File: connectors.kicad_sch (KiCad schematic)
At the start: 4 parts

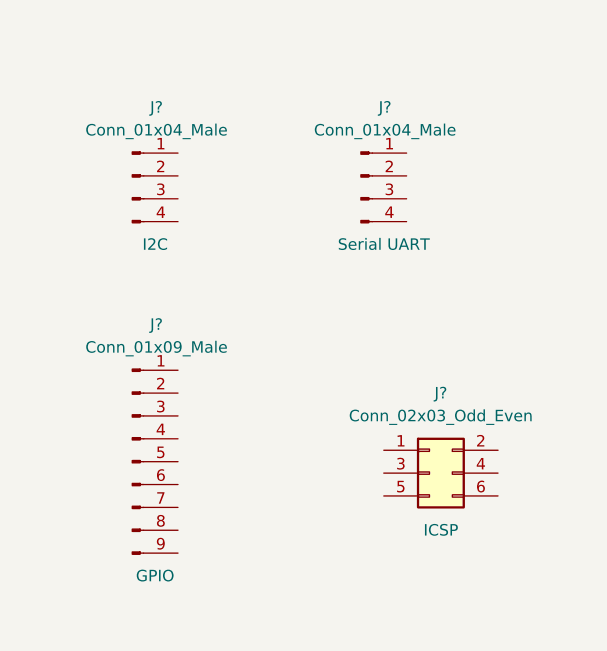
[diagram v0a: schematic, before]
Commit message: Changed locations of symbols (arrange).
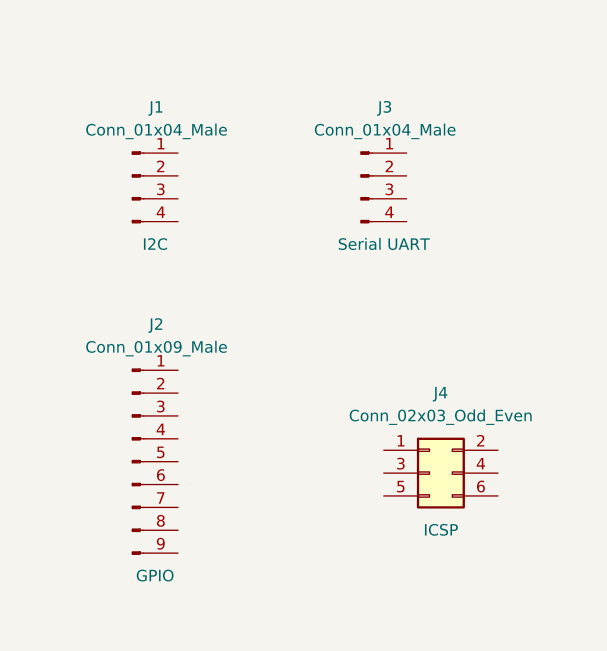
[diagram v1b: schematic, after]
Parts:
- gave numbers to parts that had none: 4
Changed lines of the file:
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@@
   (symbol (lib_id "Connector:Conn_01x04_Male") (at 116.84 78.74 0) (unit 1)
     (in_bom yes) (on_board yes)
-    (property "Reference" "J?" (id 0) (at 119.5324 71.12 0))
+    (property "Reference" "J1" (id 0) (at 119.5324 71.12 0))
     (property "Value" "Conn_01x04_Male" (id 1) (at 119.5324 73.66 0))
     (property "Footprint" "" (id 2) (at 116.84 78.74 0)
@@
   (symbol (lib_id "Connector:Conn_01x04_Male") (at 142.24 78.74 0) (unit 1)
     (in_bom yes) (on_board yes)
-    (property "Reference" "J?" (id 0) (at 144.9324 71.12 0))
+    (property "Reference" "J3" (id 0) (at 144.9324 71.12 0))
     (property "Value" "Conn_01x04_Male" (id 1) (at 144.9324 73.66 0))
     (property "Footprint" "" (id 2) (at 142.24 78.74 0)
@@
   (symbol (lib_id "Connector_Generic:Conn_02x03_Odd_Even") (at 149.86 111.76 0) (unit 1)
     (in_bom yes) (on_board yes)
-    (property "Reference" "J?" (id 0) (at 151.13 102.87 0))
+    (property "Reference" "J4" (id 0) (at 151.13 102.87 0))
     (property "Value" "Conn_02x03_Odd_Even" (id 1) (at 151.13 105.41 0))
     (property "Footprint" "" (id 2) (at 149.86 111.76 0)
@@
   (symbol (lib_id "Connector:Conn_01x09_Male") (at 116.84 110.49 0) (unit 1)
     (in_bom yes) (on_board yes)
-    (property "Reference" "J?" (id 0) (at 119.5324 95.25 0))
+    (property "Reference" "J2" (id 0) (at 119.5324 95.25 0))
     (property "Value" "Conn_01x09_Male" (id 1) (at 119.5324 97.79 0))
     (property "Footprint" "" (id 2) (at 116.84 110.49 0)

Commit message: Completed symbol-footprint associations.
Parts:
- J1, J3: footprint (none) -> Connector_PinHeader_2.54mm:PinHeader_1x04_P2.54mm_Vertical
- J2: footprint (none) -> Connector_PinHeader_2.54mm:PinHeader_1x09_P2.54mm_Vertical
- J4: footprint (none) -> Connector_PinHeader_2.54mm:PinHeader_2x03_P2.54mm_Vertical
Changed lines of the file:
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@@
     (property "Reference" "J1" (id 0) (at 119.5324 71.12 0))
     (property "Value" "Conn_01x04_Male" (id 1) (at 119.5324 73.66 0))
-    (property "Footprint" "" (id 2) (at 116.84 78.74 0)
+    (property "Footprint" "Connector_PinHeader_2.54mm:PinHeader_1x04_P2.54mm_Vertical" (id 2) (at 116.84 78.74 0)
       (effects (font (size 1.27 1.27)) hide)
     )
@@
     (property "Reference" "J3" (id 0) (at 144.9324 71.12 0))
     (property "Value" "Conn_01x04_Male" (id 1) (at 144.9324 73.66 0))
-    (property "Footprint" "" (id 2) (at 142.24 78.74 0)
+    (property "Footprint" "Connector_PinHeader_2.54mm:PinHeader_1x04_P2.54mm_Vertical" (id 2) (at 142.24 78.74 0)
       (effects (font (size 1.27 1.27)) hide)
     )
@@
     (property "Reference" "J4" (id 0) (at 151.13 102.87 0))
     (property "Value" "Conn_02x03_Odd_Even" (id 1) (at 151.13 105.41 0))
-    (property "Footprint" "" (id 2) (at 149.86 111.76 0)
+    (property "Footprint" "Connector_PinHeader_2.54mm:PinHeader_2x03_P2.54mm_Vertical" (id 2) (at 149.86 111.76 0)
       (effects (font (size 1.27 1.27)) hide)
     )
@@
     (property "Reference" "J2" (id 0) (at 119.5324 95.25 0))
     (property "Value" "Conn_01x09_Male" (id 1) (at 119.5324 97.79 0))
-    (property "Footprint" "" (id 2) (at 116.84 110.49 0)
+    (property "Footprint" "Connector_PinHeader_2.54mm:PinHeader_1x09_P2.54mm_Vertical" (id 2) (at 116.84 110.49 0)
       (effects (font (size 1.27 1.27)) hide)
     )

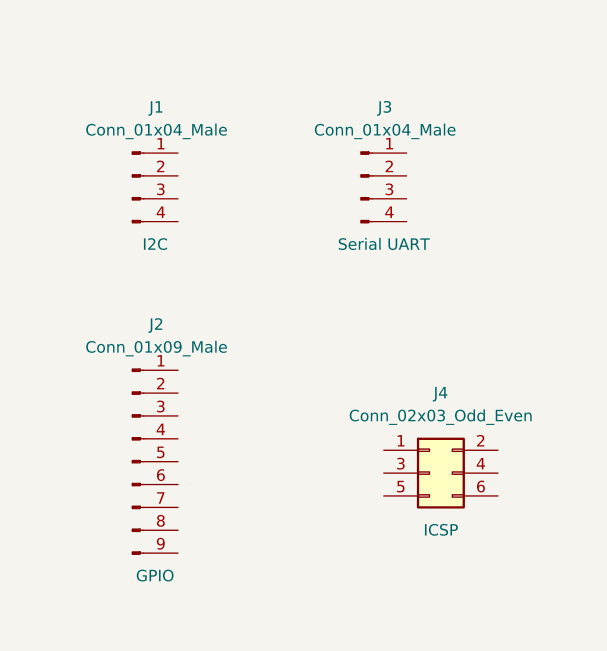
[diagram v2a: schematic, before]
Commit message: Completed wiring in the second sheet.
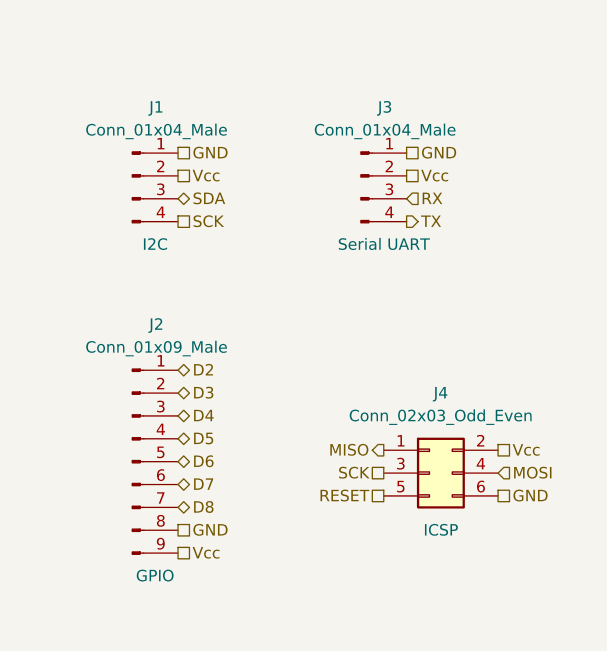
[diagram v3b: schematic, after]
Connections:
- net MISO: now reaches J4.1 (Pin_1)
- net Vcc: now reaches J4.2 (Pin_2)
- net Vcc: now also J1.2 (Pin_2), J2.9 (Pin_9), J3.2 (Pin_2)
- net SCK: now reaches J4.3 (Pin_3)
- net SCK: now also J1.4 (Pin_4)
- net MOSI: now reaches J4.4 (Pin_4)
- net RESET: now reaches J4.5 (Pin_5)
- net GND: now reaches J4.6 (Pin_6)
- net GND: now also J1.1 (Pin_1), J2.8 (Pin_8), J3.1 (Pin_1)
- net D2: now reaches J2.1 (Pin_1)
- net D3: now reaches J2.2 (Pin_2)
- net D4: now reaches J2.3 (Pin_3)
- net D5: now reaches J2.4 (Pin_4)
- net D6: now reaches J2.5 (Pin_5)
- net D7: now reaches J2.6 (Pin_6)
- net D8: now reaches J2.7 (Pin_7)
- net RX: now reaches J3.3 (Pin_3)
- net TX: now reaches J3.4 (Pin_4)
- net SDA: now reaches J1.3 (Pin_3)
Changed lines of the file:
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@@
 (kicad_sch (version 20210621) (generator eeschema)
   (paper "A4")
+  (hierarchical_label "GND" (shape passive) (at 121.92 76.2 0)
+    (effects (font (size 1.27 1.27)) (justify left))
+  )
+  (hierarchical_label "Vcc" (shape passive) (at 121.92 78.74 0)
+    (effects (font (size 1.27 1.27)) (justify left))
+  )
+  (hierarchical_label "SDA" (shape bidirectional) (at 121.92 81.28 0)
+    (effects (font (size 1.27 1.27)) (justify left))
+  )
+  (hierarchical_label "SCK" (shape passive) (at 121.92 83.82 0)
+    (effects (font (size 1.27 1.27)) (justify left))
+  )
+  (hierarchical_label "D2" (shape bidirectional) (at 121.92 100.33 0)
+    (effects (font (size 1.27 1.27)) (justify left))
+  )
+  (hierarchical_label "D3" (shape bidirectional) (at 121.92 102.87 0)
+    (effects (font (size 1.27 1.27)) (justify left))
+  )
+  (hierarchical_label "D4" (shape bidirectional) (at 121.92 105.41 0)
+    (effects (font (size 1.27 1.27)) (justify left))
+  )
+  (hierarchical_label "D5" (shape bidirectional) (at 121.92 107.95 0)
+    (effects (font (size 1.27 1.27)) (justify left))
+  )
+  (hierarchical_label "D6" (shape bidirectional) (at 121.92 110.49 0)
+    (effects (font (size 1.27 1.27)) (justify left))
+  )
+  (hierarchical_label "D7" (shape bidirectional) (at 121.92 113.03 0)
+    (effects (font (size 1.27 1.27)) (justify left))
+  )
+  (hierarchical_label "D8" (shape bidirectional) (at 121.92 115.57 0)
+    (effects (font (size 1.27 1.27)) (justify left))
+  )
+  (hierarchical_label "GND" (shape passive) (at 121.92 118.11 0)
+    (effects (font (size 1.27 1.27)) (justify left))
+  )
+  (hierarchical_label "Vcc" (shape passive) (at 121.92 120.65 0)
+    (effects (font (size 1.27 1.27)) (justify left))
+  )
+  (hierarchical_label "MISO" (shape output) (at 144.78 109.22 180)
+    (effects (font (size 1.27 1.27)) (justify right))
+  )
+  (hierarchical_label "SCK" (shape passive) (at 144.78 111.76 180)
+    (effects (font (size 1.27 1.27)) (justify right))
+  )
+  (hierarchical_label "RESET" (shape passive) (at 144.78 114.3 180)
+    (effects (font (size 1.27 1.27)) (justify right))
+  )
+  (hierarchical_label "GND" (shape passive) (at 147.32 76.2 0)
+    (effects (font (size 1.27 1.27)) (justify left))
+  )
+  (hierarchical_label "Vcc" (shape passive) (at 147.32 78.74 0)
+    (effects (font (size 1.27 1.27)) (justify left))
+  )
+  (hierarchical_label "RX" (shape input) (at 147.32 81.28 0)
+    (effects (font (size 1.27 1.27)) (justify left))
+  )
+  (hierarchical_label "TX" (shape output) (at 147.32 83.82 0)
+    (effects (font (size 1.27 1.27)) (justify left))
+  )
+  (hierarchical_label "Vcc" (shape passive) (at 157.48 109.22 0)
+    (effects (font (size 1.27 1.27)) (justify left))
+  )
+  (hierarchical_label "MOSI" (shape input) (at 157.48 111.76 0)
+    (effects (font (size 1.27 1.27)) (justify left))
+  )
+  (hierarchical_label "GND" (shape passive) (at 157.48 114.3 0)
+    (effects (font (size 1.27 1.27)) (justify left))
+  )
   (symbol (lib_id "Connector:Conn_01x04_Male") (at 116.84 78.74 0) (unit 1)
     (in_bom yes) (on_board yes)

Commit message: Fixed errata #106
I2C clock should be named SCL and not connected to SPI click net SCK
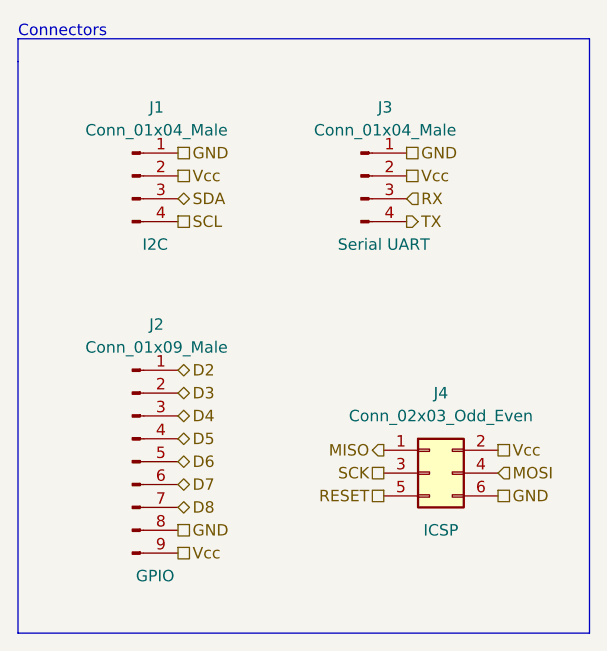
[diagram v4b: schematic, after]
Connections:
- net SCK: no longer J1.4 (Pin_4)
- new net SCL: J1.4 (Pin_4)
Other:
- note added: "Connectors"
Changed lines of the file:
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@@
-(kicad_sch (version 20210621) (generator eeschema)
+(kicad_sch (version 20211123) (generator eeschema)
   (paper "A4")
+  (polyline (pts (xy 104.14 63.5) (xy 104.14 66.04))
+    (stroke (width 0) (type default) (color 0 0 0 0))
+  )
+  (polyline (pts (xy 104.14 66.04) (xy 104.14 129.54))
+    (stroke (width 0) (type default) (color 0 0 0 0))
+  )
+  (polyline (pts (xy 104.14 129.54) (xy 167.64 129.54))
+    (stroke (width 0) (type default) (color 0 0 0 0))
+  )
+  (polyline (pts (xy 167.64 63.5) (xy 104.14 63.5))
+    (stroke (width 0) (type default) (color 0 0 0 0))
+  )
+  (polyline (pts (xy 167.64 129.54) (xy 167.64 63.5))
+    (stroke (width 0) (type default) (color 0 0 0 0))
+  )
+  (text "Connectors" (at 104.14 63.5 0)
+    (effects (font (size 1.27 1.27)) (justify left bottom))
+  )
   (hierarchical_label "GND" (shape passive) (at 121.92 76.2 0)
     (effects (font (size 1.27 1.27)) (justify left))
@@
     (effects (font (size 1.27 1.27)) (justify left))
   )
+  (hierarchical_label "Vcc" (shape passive) (at 147.32 78.74 0)
+    (effects (font (size 1.27 1.27)) (justify left))
+  )
+  (hierarchical_label "SCL" (shape passive) (at 121.92 83.82 0)
+    (effects (font (size 1.27 1.27)) (justify left))
+  )
+  (hierarchical_label "Vcc" (shape passive) (at 121.92 120.65 0)
+    (effects (font (size 1.27 1.27)) (justify left))
+  )
+  (hierarchical_label "D6" (shape bidirectional) (at 121.92 110.49 0)
+    (effects (font (size 1.27 1.27)) (justify left))
+  )
+  (hierarchical_label "SCK" (shape passive) (at 144.78 111.76 180)
+    (effects (font (size 1.27 1.27)) (justify right))
+  )
+  (hierarchical_label "MISO" (shape output) (at 144.78 109.22 180)
+    (effects (font (size 1.27 1.27)) (justify right))
+  )
+  (hierarchical_label "GND" (shape passive) (at 147.32 76.2 0)
+    (effects (font (size 1.27 1.27)) (justify left))
+  )
+  (hierarchical_label "D3" (shape bidirectional) (at 121.92 102.87 0)
+    (effects (font (size 1.27 1.27)) (justify left))
+  )
+  (hierarchical_label "TX" (shape output) (at 147.32 83.82 0)
+    (effects (font (size 1.27 1.27)) (justify left))
+  )
   (hierarchical_label "SDA" (shape bidirectional) (at 121.92 81.28 0)
     (effects (font (size 1.27 1.27)) (justify left))
   )
-  (hierarchical_label "SCK" (shape passive) (at 121.92 83.82 0)
+  (hierarchical_label "GND" (shape passive) (at 157.48 114.3 0)
+    (effects (font (size 1.27 1.27)) (justify left))
+  )
+  (hierarchical_label "D4" (shape bidirectional) (at 121.92 105.41 0)
+    (effects (font (size 1.27 1.27)) (justify left))
+  )
+  (hierarchical_label "GND" (shape passive) (at 121.92 118.11 0)
+    (effects (font (size 1.27 1.27)) (justify left))
+  )
+  (hierarchical_label "D7" (shape bidirectional) (at 121.92 113.03 0)
+    (effects (font (size 1.27 1.27)) (justify left))
+  )
+  (hierarchical_label "Vcc" (shape passive) (at 157.48 109.22 0)
     (effects (font (size 1.27 1.27)) (justify left))
   )
@@
     (effects (font (size 1.27 1.27)) (justify left))
   )
-  (hierarchical_label "D3" (shape bidirectional) (at 121.92 102.87 0)
-    (effects (font (size 1.27 1.27)) (justify left))
-  )
-  (hierarchical_label "D4" (shape bidirectional) (at 121.92 105.41 0)
-    (effects (font (size 1.27 1.27)) (justify left))
-  )
-  (hierarchical_label "D5" (shape bidirectional) (at 121.92 107.95 0)
-    (effects (font (size 1.27 1.27)) (justify left))
-  )
-  (hierarchical_label "D6" (shape bidirectional) (at 121.92 110.49 0)
-    (effects (font (size 1.27 1.27)) (justify left))
-  )
-  (hierarchical_label "D7" (shape bidirectional) (at 121.92 113.03 0)
-    (effects (font (size 1.27 1.27)) (justify left))
-  )
-  (hierarchical_label "D8" (shape bidirectional) (at 121.92 115.57 0)
-    (effects (font (size 1.27 1.27)) (justify left))
-  )
-  (hierarchical_label "GND" (shape passive) (at 121.92 118.11 0)
-    (effects (font (size 1.27 1.27)) (justify left))
-  )
-  (hierarchical_label "Vcc" (shape passive) (at 121.92 120.65 0)
-    (effects (font (size 1.27 1.27)) (justify left))
-  )
-  (hierarchical_label "MISO" (shape output) (at 144.78 109.22 180)
-    (effects (font (size 1.27 1.27)) (justify right))
-  )
-  (hierarchical_label "SCK" (shape passive) (at 144.78 111.76 180)
-    (effects (font (size 1.27 1.27)) (justify right))
-  )
   (hierarchical_label "RESET" (shape passive) (at 144.78 114.3 180)
     (effects (font (size 1.27 1.27)) (justify right))
   )
-  (hierarchical_label "GND" (shape passive) (at 147.32 76.2 0)
-    (effects (font (size 1.27 1.27)) (justify left))
-  )
-  (hierarchical_label "Vcc" (shape passive) (at 147.32 78.74 0)
+  (hierarchical_label "D8" (shape bidirectional) (at 121.92 115.57 0)
     (effects (font (size 1.27 1.27)) (justify left))
   )
@@
     (effects (font (size 1.27 1.27)) (justify left))
   )
-  (hierarchical_label "TX" (shape output) (at 147.32 83.82 0)
-    (effects (font (size 1.27 1.27)) (justify left))
-  )
-  (hierarchical_label "Vcc" (shape passive) (at 157.48 109.22 0)
-    (effects (font (size 1.27 1.27)) (justify left))
-  )
   (hierarchical_label "MOSI" (shape input) (at 157.48 111.76 0)
     (effects (font (size 1.27 1.27)) (justify left))
   )
-  (hierarchical_label "GND" (shape passive) (at 157.48 114.3 0)
+  (hierarchical_label "D5" (shape bidirectional) (at 121.92 107.95 0)
     (effects (font (size 1.27 1.27)) (justify left))
-  )
-  (symbol (lib_id "Connector:Conn_01x04_Male") (at 116.84 78.74 0) (unit 1)
-    (in_bom yes) (on_board yes)
-    (property "Reference" "J1" (id 0) (at 119.5324 71.12 0))
-    (property "Value" "Conn_01x04_Male" (id 1) (at 119.5324 73.66 0))
-    (property "Footprint" "Connector_PinHeader_2.54mm:PinHeader_1x04_P2.54mm_Vertical" (id 2) (at 116.84 78.74 0)
-      (effects (font (size 1.27 1.27)) hide)
-    )
-    (property "Datasheet" "~" (id 3) (at 116.84 78.74 0)
-      (effects (font (size 1.27 1.27)) hide)
-    )
-    (property "Purpose" "I2C" (id 4) (at 119.38 86.36 0))
-    (pin "1")
-    (pin "2")
-    (pin "3")
-    (pin "4")
-  )
-  (symbol (lib_id "Connector:Conn_01x04_Male") (at 142.24 78.74 0) (unit 1)
-    (in_bom yes) (on_board yes)
-    (property "Reference" "J3" (id 0) (at 144.9324 71.12 0))
-    (property "Value" "Conn_01x04_Male" (id 1) (at 144.9324 73.66 0))
-    (property "Footprint" "Connector_PinHeader_2.54mm:PinHeader_1x04_P2.54mm_Vertical" (id 2) (at 142.24 78.74 0)
-      (effects (font (size 1.27 1.27)) hide)
-    )
-    (property "Datasheet" "~" (id 3) (at 142.24 78.74 0)
-      (effects (font (size 1.27 1.27)) hide)
-    )
-    (property "Purpose" "Serial UART" (id 4) (at 144.78 86.36 0))
-    (pin "1")
-    (pin "2")
-    (pin "3")
-    (pin "4")
   )
   (symbol (lib_id "Connector_Generic:Conn_02x03_Odd_Even") (at 149.86 111.76 0) (unit 1)
@@
     (pin "9")
   )
+  (symbol (lib_id "Connector:Conn_01x04_Male") (at 142.24 78.74 0) (unit 1)
+    (in_bom yes) (on_board yes)
+    (property "Reference" "J3" (id 0) (at 144.9324 71.12 0))
+    (property "Value" "Conn_01x04_Male" (id 1) (at 144.9324 73.66 0))
+    (property "Footprint" "Connector_PinHeader_2.54mm:PinHeader_1x04_P2.54mm_Vertical" (id 2) (at 142.24 78.74 0)
+      (effects (font (size 1.27 1.27)) hide)
+    )
+    (property "Datasheet" "~" (id 3) (at 142.24 78.74 0)
+      (effects (font (size 1.27 1.27)) hide)
+    )
+    (property "Purpose" "Serial UART" (id 4) (at 144.78 86.36 0))
+    (pin "1")
+    (pin "2")
+    (pin "3")
+    (pin "4")
+  )
+  (symbol (lib_id "Connector:Conn_01x04_Male") (at 116.84 78.74 0) (unit 1)
+    (in_bom yes) (on_board yes)
+    (property "Reference" "J1" (id 0) (at 119.5324 71.12 0))
+    (property "Value" "Conn_01x04_Male" (id 1) (at 119.5324 73.66 0))
+    (property "Footprint" "Connector_PinHeader_2.54mm:PinHeader_1x04_P2.54mm_Vertical" (id 2) (at 116.84 78.74 0)
+      (effects (font (size 1.27 1.27)) hide)
+    )
+    (property "Datasheet" "~" (id 3) (at 116.84 78.74 0)
+      (effects (font (size 1.27 1.27)) hide)
+    )
+    (property "Purpose" "I2C" (id 4) (at 119.38 86.36 0))
+    (pin "1")
+    (pin "2")
+    (pin "3")
+    (pin "4")
+  )
 )
